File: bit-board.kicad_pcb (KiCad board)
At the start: 4 copper layers, 85 x 56 mm, 209 parts, among them M1 FDV301N, M1A NX3008PBK, M1B2 FDV301N, M1B3 FDV301N, M1BF NX3008PBK, M1BG NX3008PBK, M1DE FDV301N, M1L0 FDV301N, M1L1 FDV301N, M1L2 FDV301N, M1L3 FDV301N, M1MAG FDV301N, M1NAF FDV301N, M1NAG FDV301N, M1NEE FDV301N, M1NL FDV301N, M1NS4 FDV301N, M1OEE FDV301N, M1ON FDV301N, M1S5 FDV301N, M1S6 FDV301N, M1S7 FDV301N, M1S8 FDV301N, M1S9 FDV301N, M1XE FDV301N, M2 FDV301N, M2A FDV301N, M2B2 NX3008PBK, M2B3 NX3008PBK, M2BF FDV301N, M2BG FDV301N, M2DE FDV301N, M2L0 FDV301N, M2L1 FDV301N, M2L2 FDV301N, M2L3 FDV301N, M2MAG FDV301N, M2NAF FDV301N, M2NAG FDV301N, M2NEE FDV301N, M2NL FDV301N, M2NS4 FDV301N, M2OEE FDV301N, M2ON FDV301N, M2S5 FDV301N, M2S6 FDV301N, M2S7 FDV301N, M2S8 FDV301N, M2S9 FDV301N, M2XE FDV301N, M3 FDV301N, M3A NX3008PBK, M3BF NX3008PBK, M3BG NX3008PBK, M3OEE FDV301N, M3ON FDV301N, M3XE FDV301N, M4 FDV301N, M4A FDV301N, M4BF FDV301N, M4BG FDV301N, M4XE FDV301N, Q1BF PDTC124TU, Q1BG PDTC124TU, Q1K PDTC124TU, Q1L0 PDTC124TU, Q1L1 PDTC124TU, Q1L2 PDTC124TU, Q1L3 PDTC124TU, Q1R PDTC124TU, Q1U PDTC124TU, Q1X PDTC124TU, Q1Y PDTC124TU, Q2A PDTC124TU, Q2BF PDTC124TU, Q2BG PDTC124TU, Q2K PDTC124TU, Q2L0 PDTC124TU, Q2L1 PDTC124TU, Q2L2 PDTC124TU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

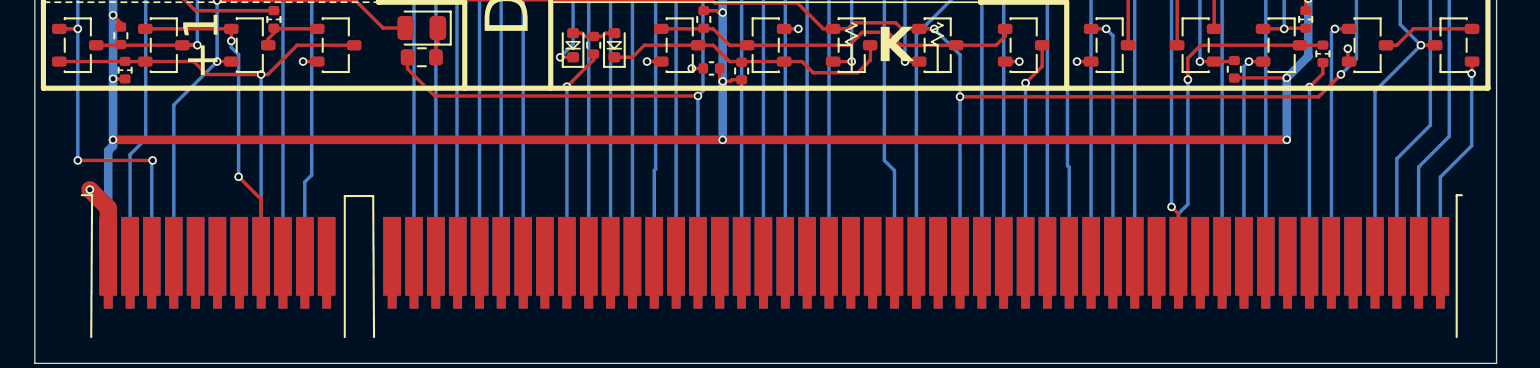
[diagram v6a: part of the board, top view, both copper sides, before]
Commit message: Add more ground and power on the bit edge connector.
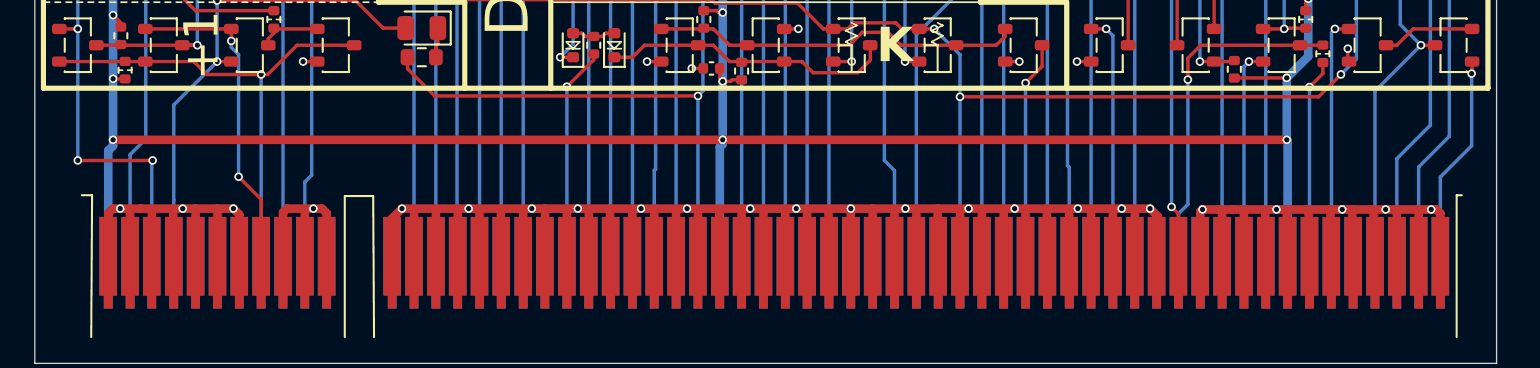
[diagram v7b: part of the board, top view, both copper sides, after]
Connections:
- JMAIN pad A29: (no net) -> Vdd
- JMAIN pad A55: (no net) -> Vdd
- JMAIN pad B10: (no net) -> GND
- JMAIN pad B11: (no net) -> GND
- JMAIN pad B14: (no net) -> GND
- JMAIN pad B15: (no net) -> GND
- JMAIN pad B16: (no net) -> GND
- JMAIN pad B17: (no net) -> GND
- JMAIN pad B18: (no net) -> GND
- JMAIN pad B19: (no net) -> GND
- JMAIN pad B2: (no net) -> GND
- JMAIN pad B20: (no net) -> GND
- JMAIN pad B21: (no net) -> GND
- JMAIN pad B22: (no net) -> GND
- JMAIN pad B23: (no net) -> GND
- JMAIN pad B24: (no net) -> GND
- JMAIN pad B25: (no net) -> GND
- JMAIN pad B26: (no net) -> GND
- JMAIN pad B27: (no net) -> GND
- JMAIN pad B28: (no net) -> GND
- JMAIN pad B29: (no net) -> GND
- JMAIN pad B3: (no net) -> GND
- JMAIN pad B30: (no net) -> GND
- JMAIN pad B31: (no net) -> GND
- JMAIN pad B32: (no net) -> GND
- JMAIN pad B33: (no net) -> GND
- JMAIN pad B34: (no net) -> GND
- JMAIN pad B35: (no net) -> GND
- JMAIN pad B36: (no net) -> GND
- JMAIN pad B37: (no net) -> GND
- JMAIN pad B38: (no net) -> GND
- JMAIN pad B39: (no net) -> GND
- JMAIN pad B4: (no net) -> GND
- JMAIN pad B40: (no net) -> GND
- JMAIN pad B41: (no net) -> GND
- JMAIN pad B42: (no net) -> GND
- JMAIN pad B43: (no net) -> GND
- JMAIN pad B44: (no net) -> GND
- JMAIN pad B45: (no net) -> GND
- JMAIN pad B46: (no net) -> GND
- JMAIN pad B47: (no net) -> GND
- JMAIN pad B48: (no net) -> GND
- JMAIN pad B49: (no net) -> GND
- JMAIN pad B5: (no net) -> GND
- JMAIN pad B51: (no net) -> GND
- JMAIN pad B52: (no net) -> GND
- JMAIN pad B53: (no net) -> GND
- JMAIN pad B54: (no net) -> GND
- JMAIN pad B55: (no net) -> GND
- JMAIN pad B56: (no net) -> GND
- JMAIN pad B57: (no net) -> GND
- JMAIN pad B58: (no net) -> GND
- JMAIN pad B59: (no net) -> GND
- JMAIN pad B6: (no net) -> GND
- JMAIN pad B60: (no net) -> GND
- JMAIN pad B61: (no net) -> GND
- JMAIN pad B62: (no net) -> GND
- JMAIN pad B7: (no net) -> GND
- JMAIN pad B9: (no net) -> GND
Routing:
- net GND: track 64.7 -> 288.0 mm, vias 77 -> 100
- net Vdd: track 352.1 -> 365.7 mm

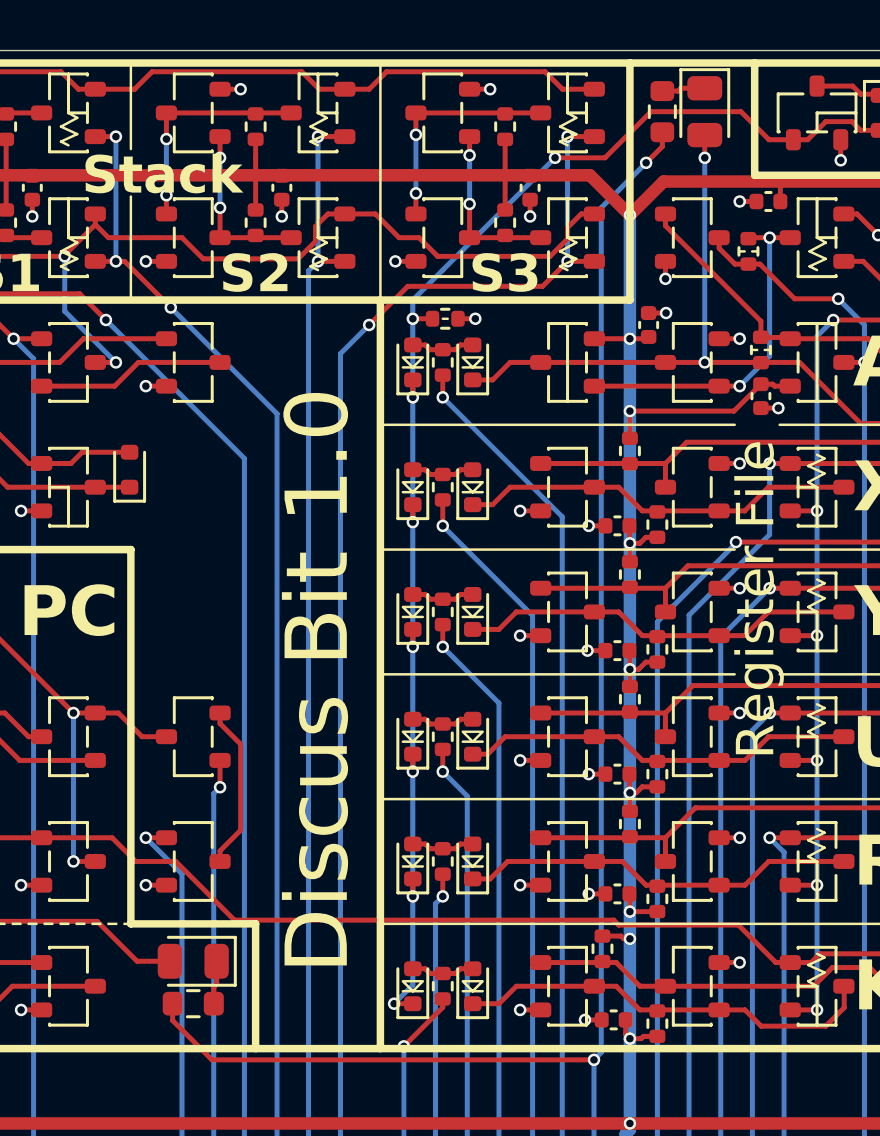
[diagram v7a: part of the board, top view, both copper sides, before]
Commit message: Correct led polarity.
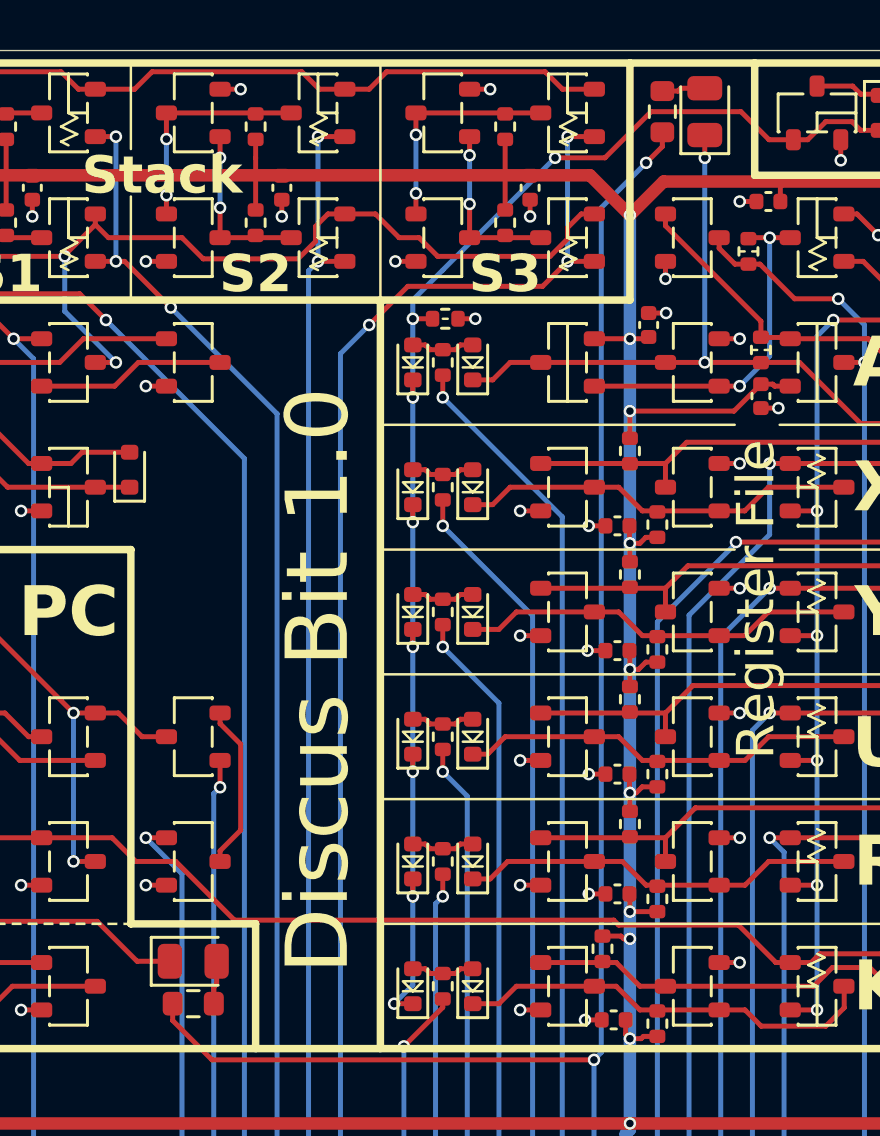
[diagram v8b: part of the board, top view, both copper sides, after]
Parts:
- turned D2 to 90 degrees
- turned D3 to 0 degrees
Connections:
- D2 pad 1: _d2 -> Ao#
- D2 pad 2: Ao# -> _d2
- D3 pad 1: _d3 -> P#
- D3 pad 2: P# -> _d3
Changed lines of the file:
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@@
 	(footprint "Parts:0805-diode"
 		(layer "F.Cu")
-		(at 122.5 81.5 180)
+		(at 122.5 81.5)
 		(descr "LED SMD 0805 (2012 Metric), square (rectangular) end terminal, IPC-7351 nominal, (Body size source: https://docs.google.com/spreadsheets/d/1BsfQQcO9C6DZCsRaXUlFlo91Tg2WpOkGARC1WS5S8t0/edit?usp=sharing), generated with kicad-footprint-generator")
 		(tags "LED")
@@
 		(attr smd)
 		(fp_line
-			(start 1 -0.96)
-			(end -1.685 -0.96)
+			(start -1.685 -0.96)
+			(end -1.685 0.96)
 			(stroke
 				(width 0.12)
@@
 		)
 		(fp_line
-			(start -1.685 -0.96)
-			(end -1.685 0.96)
+			(start 1 -0.96)
+			(end -1.685 -0.96)
 			(stroke
 				(width 0.12)
@@
 		)
 		(fp_line
-			(start 1 0.6)
-			(end 1 -0.6)
+			(start -1 -0.3)
+			(end -1 0.6)
 			(stroke
 				(width 0.1)
@@
 		)
 		(fp_line
-			(start 1 -0.6)
-			(end -0.7 -0.6)
+			(start -1 0.6)
+			(end 1 0.6)
 			(stroke
 				(width 0.1)
@@
 		)
 		(fp_line
-			(start -1 0.6)
-			(end 1 0.6)
+			(start 1 -0.6)
+			(end -0.7 -0.6)
 			(stroke
 				(width 0.1)
@@
 		)
 		(fp_line
-			(start -1 -0.3)
-			(end -1 0.6)
+			(start 1 0.6)
+			(end 1 -0.6)
 			(stroke
 				(width 0.1)
@@
 		)
 		(pad "1" smd roundrect
-			(at -0.9375 0 180)
+			(at -0.9375 0)
 			(size 0.975 1.4)
 			(layers "F.Cu" "F.Mask" "F.Paste")
 			(roundrect_rratio 0.25)
-			(net 118 "_d3")
+			(net 56 "P#")
 			(pinfunction "1")
 			(pintype "passive")
 		)
 		(pad "2" smd roundrect
-			(at 0.9375 0 180)
+			(at 0.9375 0)
 			(size 0.975 1.4)
 			(layers "F.Cu" "F.Mask" "F.Paste")
 			(roundrect_rratio 0.25)
-			(net 56 "P#")
+			(net 118 "_d3")
 			(pinfunction "2")
 			(pintype "passive")
@@
 	(footprint "Parts:0805-diode"
 		(layer "F.Cu")
-		(at 143 47.45 -90)
+		(at 143 47.45 90)
 		(descr "LED SMD 0805 (2012 Metric), square (rectangular) end terminal, IPC-7351 nominal, (Body size source: https://docs.google.com/spreadsheets/d/1BsfQQcO9C6DZCsRaXUlFlo91Tg2WpOkGARC1WS5S8t0/edit?usp=sharing), generated with kicad-footprint-generator")
 		(tags "LED")
@@
 		(attr smd)
 		(fp_line
-			(start -1.685 0.96)
-			(end 1 0.96)
+			(start 1 -0.96)
+			(end -1.685 -0.96)
 			(stroke
 				(width 0.12)
@@
 		)
 		(fp_line
-			(start 1 -0.96)
-			(end -1.685 -0.96)
+			(start -1.685 0.96)
+			(end 1 0.96)
 			(stroke
 				(width 0.12)
@@
 		)
 		(fp_line
-			(start -1 0.6)
-			(end 1 0.6)
+			(start 1 -0.6)
+			(end -0.7 -0.6)
 			(stroke
 				(width 0.1)
@@
 		)
 		(fp_line
-			(start 1 0.6)
-			(end 1 -0.6)
+			(start -0.7 -0.6)
+			(end -1 -0.3)
 			(stroke
 				(width 0.1)
@@
 		)
 		(fp_line
-			(start -0.7 -0.6)
-			(end -1 -0.3)
+			(start 1 0.6)
+			(end 1 -0.6)
 			(stroke
 				(width 0.1)
@@
 		)
 		(fp_line
-			(start 1 -0.6)
-			(end -0.7 -0.6)
+			(start -1 0.6)
+			(end 1 0.6)
 			(stroke
 				(width 0.1)
@@
 		)
 		(pad "1" smd roundrect
-			(at -0.9375 0 270)
+			(at -0.9375 0 90)
 			(size 0.975 1.4)
 			(layers "F.Cu" "F.Mask" "F.Paste")
 			(roundrect_rratio 0.25)
-			(net 120 "_d2")
+			(net 53 "Ao#")
 			(pinfunction "1")
 			(pintype "passive")
 		)
 		(pad "2" smd roundrect
-			(at 0.9375 0 270)
+			(at 0.9375 0 90)
 			(size 0.975 1.4)
 			(layers "F.Cu" "F.Mask" "F.Paste")
 			(roundrect_rratio 0.25)
-			(net 53 "Ao#")
+			(net 120 "_d2")
 			(pinfunction "2")
 			(pintype "passive")
